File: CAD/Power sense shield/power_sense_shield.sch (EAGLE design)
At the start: 2 parts

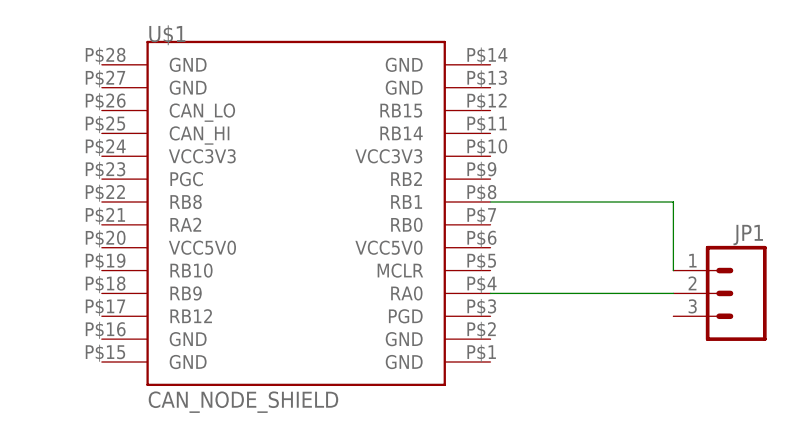
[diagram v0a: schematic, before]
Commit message: Updated the power sense board to the v3 CANode shield layout.
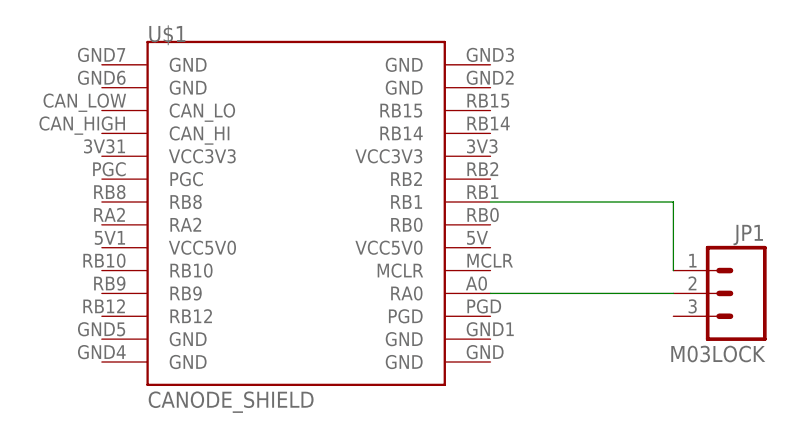
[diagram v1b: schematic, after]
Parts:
- JP1: value (none) -> M03LOCK
- U$1: value CAN_NODE_SHIELD -> CANODE_SHIELD; device ASL:CAN_NODE_SHIELD -> ASL:CANODE_SHIELD
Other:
- moved on the sheet: U$1
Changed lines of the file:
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@@
 </classes>
 <parts>
-<part name="U$1" library="ASL" deviceset="CAN_NODE_SHIELD" device=""/>
+<part name="U$1" library="ASL" deviceset="CANODE_SHIELD" device=""/>
 <part name="JP1" library="ASL" deviceset="M03" device="LOCK"/>
 </parts>
